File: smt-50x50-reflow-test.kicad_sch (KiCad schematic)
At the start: 73 parts, among them J1 Conn_01x04_Pin, J4 USB_C_Receptacle_USB2.0_14P, J8 Conn_01x04_Pin, J9 Conn_01x03_Pin, SW1 SW_Push, SW2 SW_Push, U1 ESP32-C6, U14 TMP117AIDRV, U15 BMP581, U16 TMP117AIDRV, U2 W25Q128JVS, U3 AP2112K-3.3, U4 LM317_TO-252, U7 USBLC6-2SC6, Y1 48M

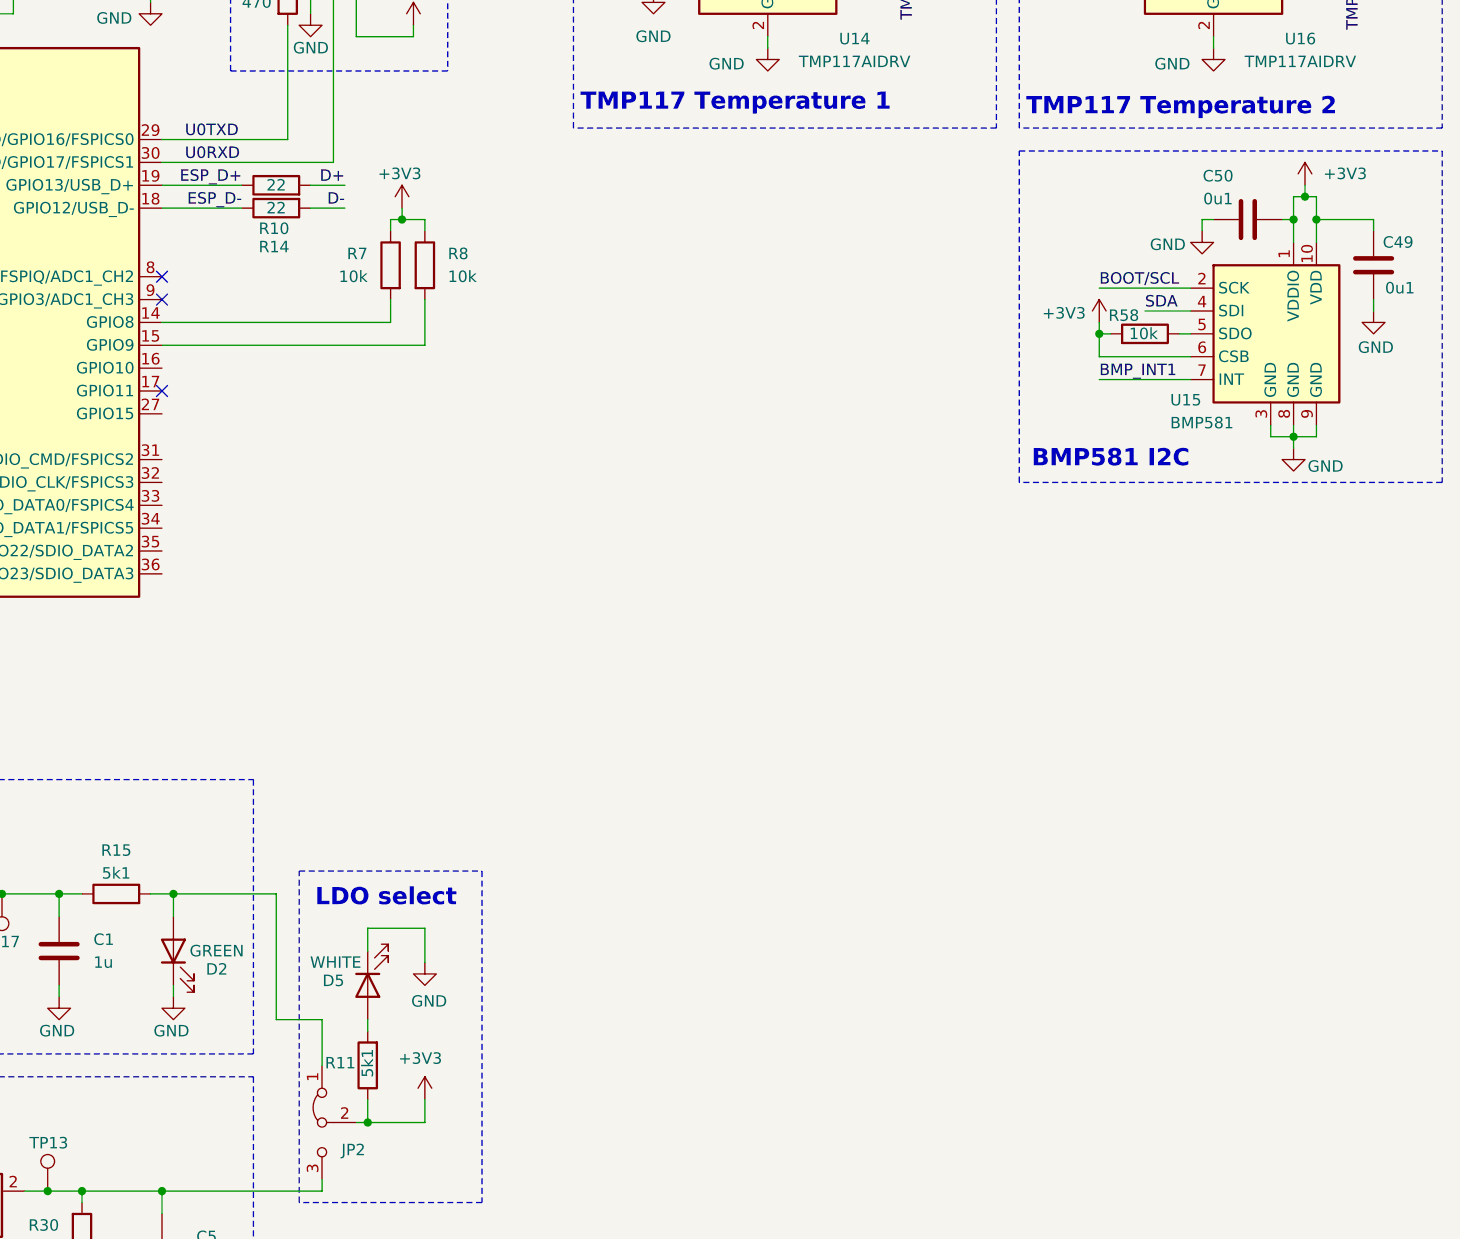
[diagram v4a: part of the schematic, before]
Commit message: schem: import LMR36520 3.5v smps from esp32c6-sensor-devboard
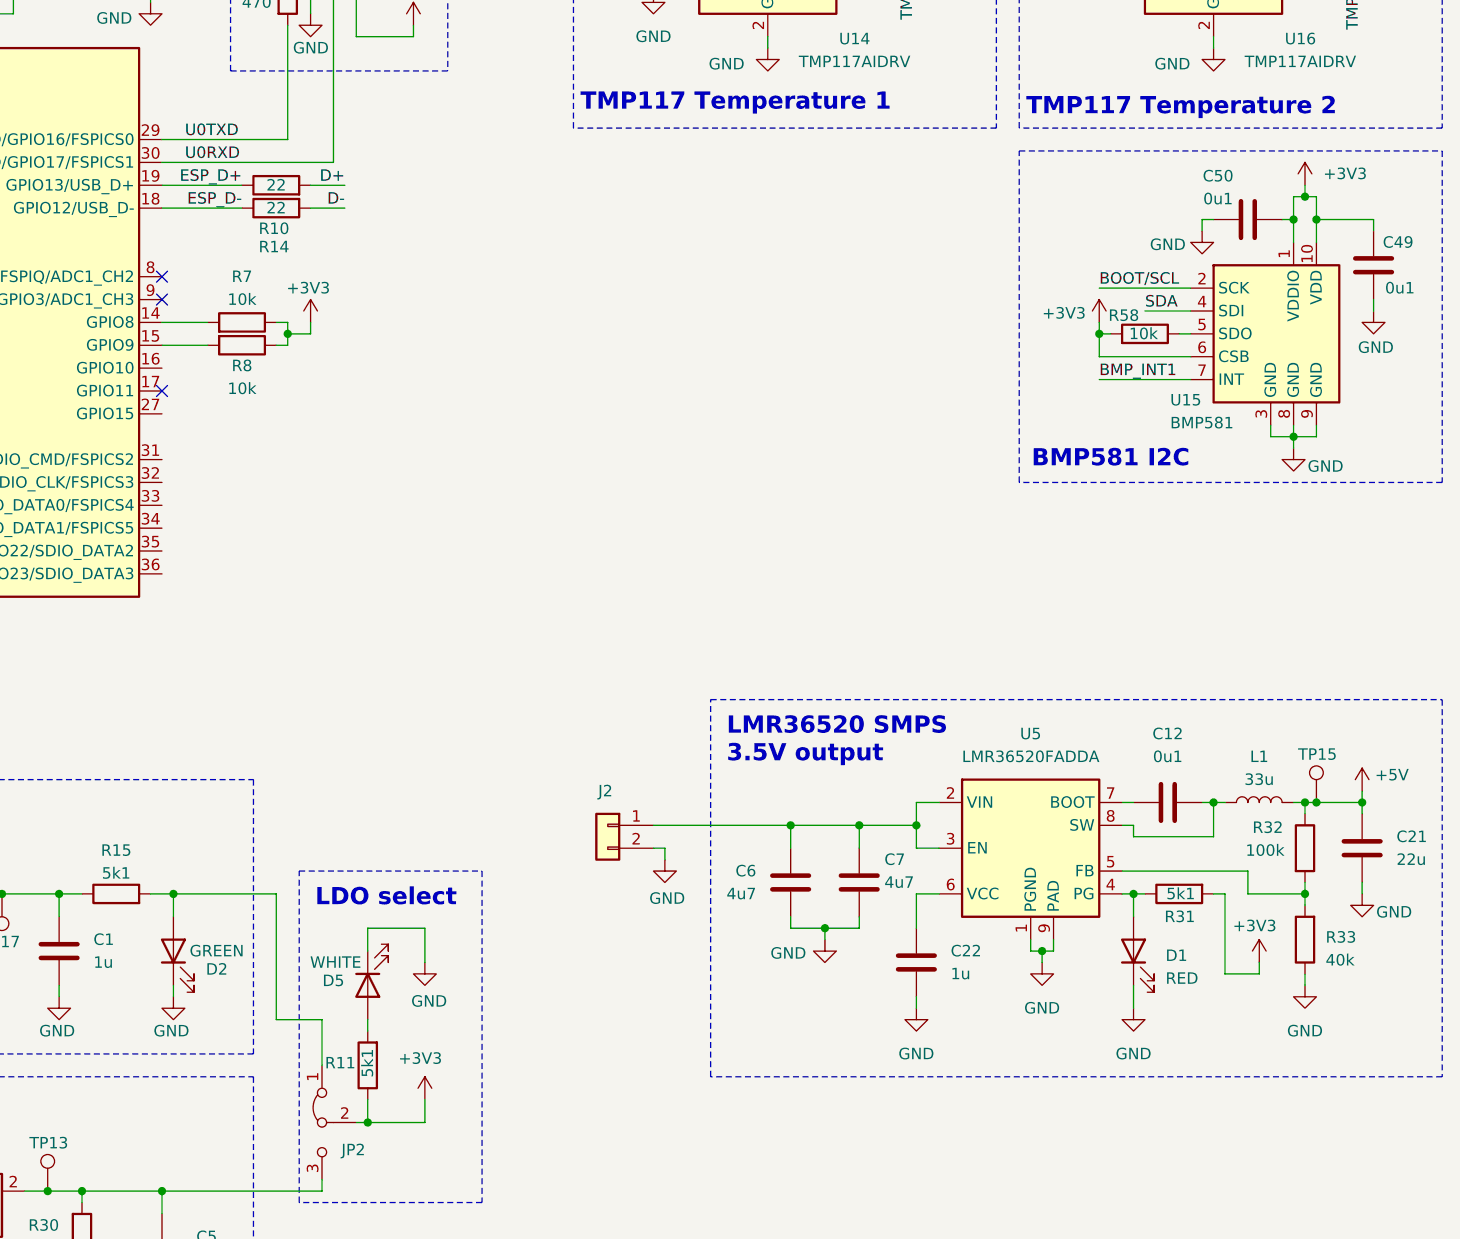
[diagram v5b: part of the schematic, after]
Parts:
- added C12: 0u1, Capacitor_SMD:C_0402_1005Metric, symbol Device:C
- added C21: 22u, Capacitor_SMD:C_0603_1608Metric, symbol Device:C
- added C22: 1u, Capacitor_SMD:C_0402_1005Metric, symbol Device:C
- added C6, C7: 4u7, Capacitor_SMD:C_1206_3216Metric, symbol Device:C
- added D1: RED, LED_SMD:LED_0603_1608Metric, symbol Device:LED
- added J2: Conn_01x02, symbol Connector_Generic:Conn_01x02
- added L1: 33u, Inductor_SMD:L_Chilisin_BMRx00060630, symbol Device:L
- added R31: 5k1, Resistor_SMD:R_0603_1608Metric, symbol Device:R
- added R32: 100k, Resistor_SMD:R_0603_1608Metric, symbol Device:R
- added R33: 40k, Resistor_SMD:R_0603_1608Metric, symbol Device:R
- added TP15: TestPoint, TestPoint:TestPoint_Pad_D2.0mm, symbol Connector:TestPoint
- added U5: LMR36520FADDA, Package_SO:Texas_HTSOP-8-1EP_3.9x4.9mm_P1.27mm_EP2.95x4.9mm_Mask2.4x3.1mm_ThermalVias, symbol Pers:LMR36520FADDA
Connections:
- net +3V3: now also R31.2
- net +5V: now also C21.2, L1.2, R32.1, TP15.1
- net GND: now also C21.1, C22.2, C6.2, C7.2, D1.1 (K), J2.2 (Pin_2), R33.1, U5.1 (PGND), U5.9 (PAD)
- new net: C6.1, C7.1, J2.1 (Pin_1), U5.2 (VIN), U5.3 (EN)
- new net: D1.2 (A), R31.1, U5.4 (PG)
- new net: R32.2, R33.2, U5.5 (FB)
- new net: C22.1, U5.6 (VCC)
- new net: C12.2, U5.7 (BOOT)
- new net: C12.1, L1.1, U5.8 (SW)
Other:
- note added: "LMR36520 SMPS 3.5V output"
- moved on the sheet: R7, R8
